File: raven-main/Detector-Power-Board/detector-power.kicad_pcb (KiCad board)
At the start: 2 copper layers, 37 x 52.5 mm, 36 parts, among them J1 DeployLipo, J2 Conn_01x06, J9 UCLipo, U1 STPS20M100SG-TR, U6 LM5185QPWPRQ1, U7 TPS7A4701xRGW, U8 TPS7A4701xRGW

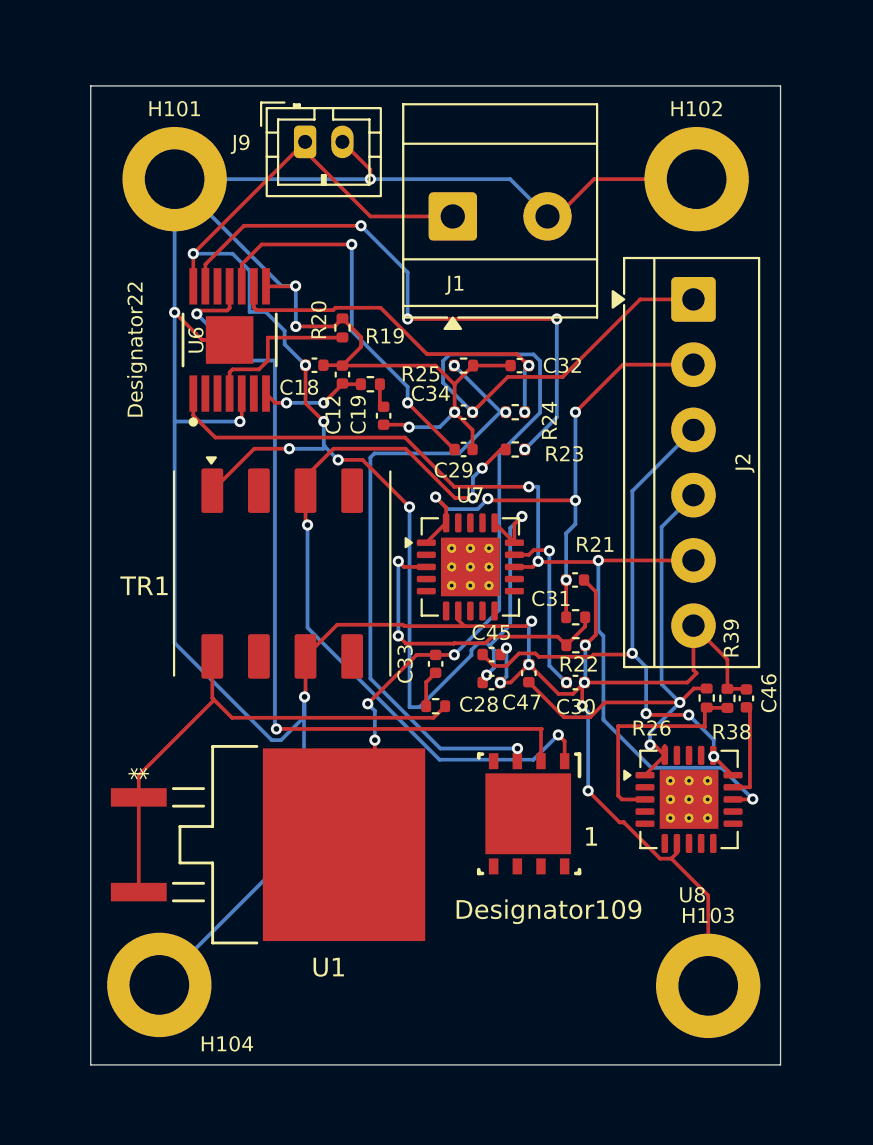
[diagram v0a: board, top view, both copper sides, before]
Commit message: Fixed Power board issues, added .step files
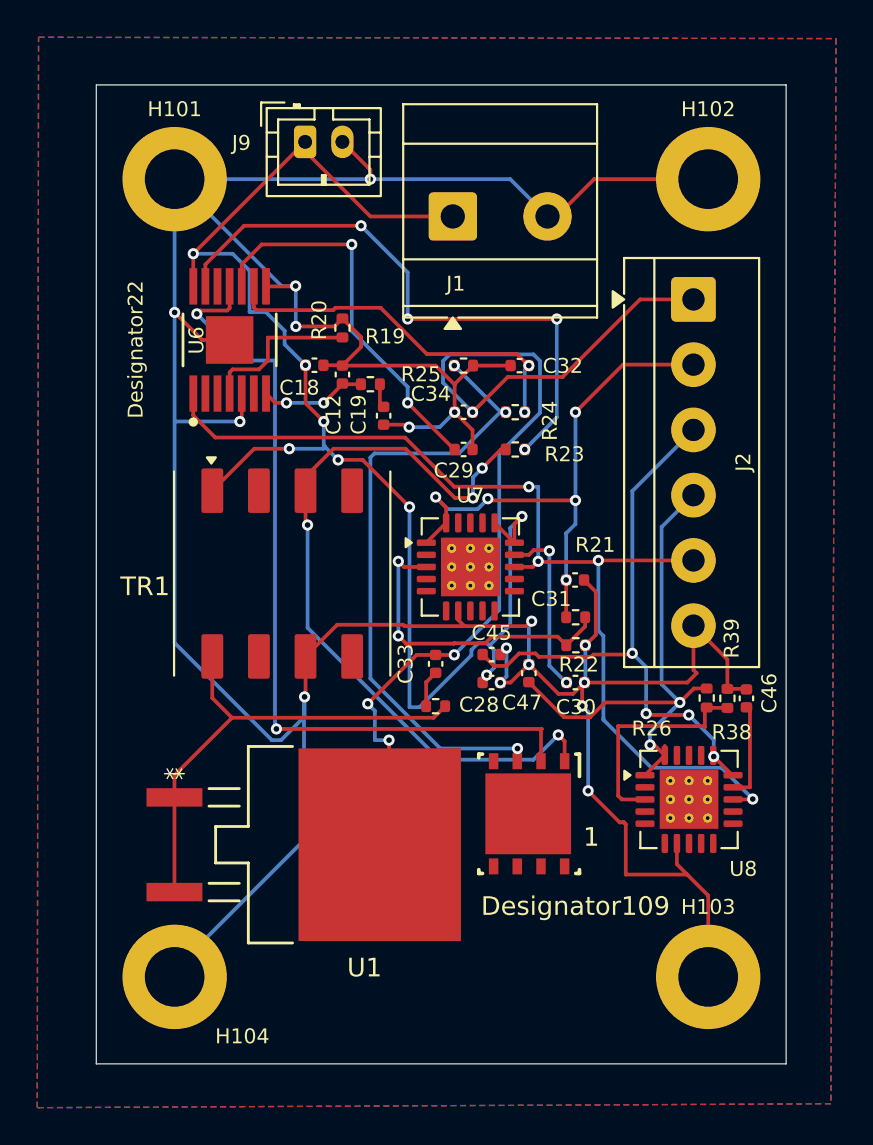
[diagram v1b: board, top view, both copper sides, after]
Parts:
- moved U1 1.91 mm to (123.8, 98.2)
- moved H104 0.93 mm to (115.0, 105.3)
- moved H102 0.62 mm to (143.6, 62.5)
- moved H103 0.48 mm to (143.6, 105.3)
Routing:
- net /Power_Out_50V: track 55.0 -> 57.7 mm
- net GND: track 201.2 -> 203.8 mm
- net Net-(R26-Pad1): track 27.4 -> 26.0 mm
- added copper zone on B.Cu, net GND
- added copper zone on F.Cu, net GND
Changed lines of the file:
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@@
 	(footprint "STPS20M100SG-TR:D2PAK_STM"
 		(layer "F.Cu")
-		(at 121.8388 98.2 -90)
+		(at 123.7521 98.2 -90)
 		(tags "STPS20M100SG-TR ")
 		(property "Reference" "U1"
@@
 		(tags "Texas VQFN NoLead")
 		(property "Reference" "U8"
-			(at 0.18 5.14 0)
+			(at 2.90875 3.72875 0)
 			(layer "F.SilkS")
 			(effects
@@
 	(footprint "MountingHole:MountingHole_3.2mm_M3_DIN965_Pad"
 		(layer "F.Cu")
-		(at 143.62 105.77)
+		(at 143.62 105.29)
 		(descr "Mounting Hole 3.2mm, M3, generated by kicad-footprint-generator mountinghole.py")
 		(tags "mountinghole M3 DIN965")
@@
 		)
 		(fp_text user "Designator109"
-			(at 5.170001 -1.045 0)
+			(at 4.960001 -2.485 0)
 			(unlocked yes)
 			(layer "F.SilkS")
@@
 	(footprint "MountingHole:MountingHole_3.2mm_M3_DIN965_Pad"
 		(layer "F.Cu")
-		(at 114.18 105.72)
+		(at 115 105.29)
 		(descr "Mounting Hole 3.2mm, M3, generated by kicad-footprint-generator mountinghole.py")
 		(tags "mountinghole M3 DIN965")
@@
 	(footprint "MountingHole:MountingHole_3.2mm_M3_DIN965_Pad"
 		(layer "F.Cu")
-		(at 143 62.5)
+		(at 143.62 62.5)
 		(descr "Mounting Hole 3.2mm, M3, generated by kicad-footprint-generator mountinghole.py")
 		(tags "mountinghole M3 DIN965")
@@
 	)
 	(gr_rect
-		(start 110.5 57.5)
-		(end 147.5 110.01)
+		(start 110.8 57.445)
+		(end 147.8 109.955)
+		(radius 5)
 		(stroke
 			(width 0.05)
-			(type default)
+			(type solid)
 		)
 		(fill no)
@@
 	)
 	(segment
+		(start 139.2 97.105432)
+		(end 139.2 99.8)
+		(width 0.2)
+		(layer "F.Cu")
+		(net "GND")
+	)
+	(segment
 		(start 144.65 89.84)
 		(end 144.65 88.27)
@@
 	)
 	(segment
+		(start 139.2 99.8)
+		(end 142.494998 99.8)
+		(width 0.2)
+		(layer "F.Cu")
+		(net "GND")
+	)
+	(segment
 		(start 130.02 73.49)
 		(end 131.01 72.5)
@@
 	)
 	(segment
-		(start 141.94125 98.646249)
-		(end 141.94125 98.13375)
-		(width 0.2)
-		(layer "F.Cu")
-		(net "GND")
-	)
-	(segment
 		(start 130.02 73.52)
 		(end 130.02 73.49)
@@
 	)
 	(segment
-		(start 141.641249 98.94625)
-		(end 143.62 100.925001)
+		(start 118.600002 75.399998)
+		(end 118.5 75.5)
 		(width 0.2)
 		(layer "F.Cu")
@@
 	)
 	(segment
-		(start 118.600002 75.399998)
-		(end 118.5 75.5)
+		(start 121.97 90.27)
+		(end 122.02 90.22)
 		(width 0.2)
 		(layer "F.Cu")
@@
 	)
 	(segment
-		(start 121.97 90.27)
-		(end 122.02 90.22)
+		(start 142.494998 99.8)
+		(end 142.497499 99.802501)
 		(width 0.2)
 		(layer "F.Cu")
@@
 	)
 	(segment
+		(start 142.497499 99.802501)
+		(end 141.94125 99.246251)
+		(width 0.2)
+		(layer "F.Cu")
+		(net "GND")
+	)
+	(segment
 		(start 130.1675 85.6625)
 		(end 130.16 85.67)
@@
 	)
 	(segment
+		(start 139.097284 97.002716)
+		(end 139.2 97.105432)
+		(width 0.2)
+		(layer "F.Cu")
+		(net "GND")
+	)
+	(segment
 		(start 137.59 84.63)
 		(end 137.59 86.94)
@@
 	)
 	(segment
-		(start 141.641249 98.94625)
-		(end 141.94125 98.646249)
-		(width 0.2)
-		(layer "F.Cu")
-		(net "GND")
-	)
-	(segment
 		(start 126.21 75.67)
 		(end 127.446671 75.67)
@@
 	)
 	(segment
-		(start 139.097284 97.002716)
-		(end 141.040818 98.94625)
-		(width 0.2)
-		(layer "F.Cu")
-		(net "GND")
-	)
-	(segment
 		(start 130.2125 85.6625)
 		(end 130.1675 85.6625)
@@
 	)
 	(segment
-		(start 141.040818 98.94625)
-		(end 141.641249 98.94625)
+		(start 130.98 75.96)
+		(end 130.02 75)
 		(width 0.2)
 		(layer "F.Cu")
@@
 	)
 	(segment
-		(start 130.98 75.96)
-		(end 130.02 75)
+		(start 141.94125 99.246251)
+		(end 141.94125 98.13375)
 		(width 0.2)
 		(layer "F.Cu")
@@
 	)
 	(segment
+		(start 143.62 100.925001)
+		(end 142.497499 99.802501)
+		(width 0.2)
+		(layer "F.Cu")
+		(net "GND")
+	)
+	(segment
 		(start 135 64.5)
 		(end 135.5 64.5)
@@
 	)
 	(segment
-		(start 117.08375 90.39625)
-		(end 117.08375 90.46625)
-		(width 0.2)
-		(layer "F.Cu")
-		(net "Net-(R26-Pad1)")
-	)
-	(segment
-		(start 128.89 91.39)
-		(end 129.51 90.77)
+		(start 117.02 90.3325)
+		(end 118.0775 91.39)
 		(width 0.2)
 		(layer "F.Cu")
@@
 	)
 	(segment
-		(start 113.0758 94.4742)
-		(end 113.0758 95.66)
+		(start 114.9891 100.74)
+		(end 114.9891 95.66)
 		(width 0.2)
 		(layer "F.Cu")
@@
 	)
 	(segment
-		(start 117.08375 90.39625)
-		(end 117.02 90.3325)
+		(start 128.89 91.39)
+		(end 129.51 90.77)
 		(width 0.2)
 		(layer "F.Cu")
@@
 	)
 	(segment
-		(start 117.08375 90.46625)
-		(end 113.0758 94.4742)
+		(start 114.9891 94.4784)
+		(end 118.0775 91.39)
 		(width 0.2)
 		(layer "F.Cu")
@@
 	)
 	(segment
-		(start 113.0758 100.74)
-		(end 113.0758 95.66)
-		(width 0.2)
-		(layer "F.Cu")
-		(net "Net-(R26-Pad1)")
-	)
-	(segment
 		(start 117.02 90.3325)
 		(end 117.02 88.1)
@@
 	)
 	(segment
-		(start 118.0775 91.39)
-		(end 117.08375 90.39625)
+		(start 114.9891 95.66)
+		(end 114.9891 94.4784)
 		(width 0.2)
 		(layer "F.Cu")
@@
 	)
 	(segment
-		(start 125.74 92.59)
-		(end 125.74 96.5467)
+		(start 126.5 97.7)
+		(end 126 98.2)
+		(width 0.2)
+		(layer "F.Cu")
+		(net "/Power_Out_50V")
+	)
+	(segment
+		(start 126.5 92.59)
+		(end 126.5 97.7)
 		(width 0.2)
 		(layer "F.Cu")
@@
 	)
 	(via
-		(at 125.74 92.59)
+		(at 125.36 90.64)
 		(size 0.6)
 		(drill 0.3)
@@
 	)
 	(via
-		(at 125.36 90.64)
+		(at 126.5 92.59)
 		(size 0.6)
 		(drill 0.3)
@@
 	)
 	(segment
+		(start 125.74 92.59)
+		(end 126.5 92.59)
+		(width 0.2)
+		(layer "B.Cu")
+		(net "/Power_Out_50V")
+	)
+	(segment
 		(start 129.4 73.42)
 		(end 129.4 72.251471)
@@
 		(net "Net-(C33-Pad1)")
 	)
+	(zone
+		(net "GND")
+		(layers "F.Cu" "B.Cu")
+		(name "Net-GND")
+		(hatch edge 0.5)
+		(connect_pads
+			(clearance 0.5)
+		)
+		(min_thickness 0.25)
+		(fill yes
+			(thermal_gap 0.5)
+			(thermal_bridge_width 0.5)
+			(island_removal_mode 0)
+		)
+		(polygon
+			(pts
+				(xy 107.7 54.89) (xy 150.48 54.96) (xy 150.201058 112.094995) (xy 107.632656 112.305037) (xy 107.7 54.9)
+			)
+		)
+	)
 	(embedded_fonts no)

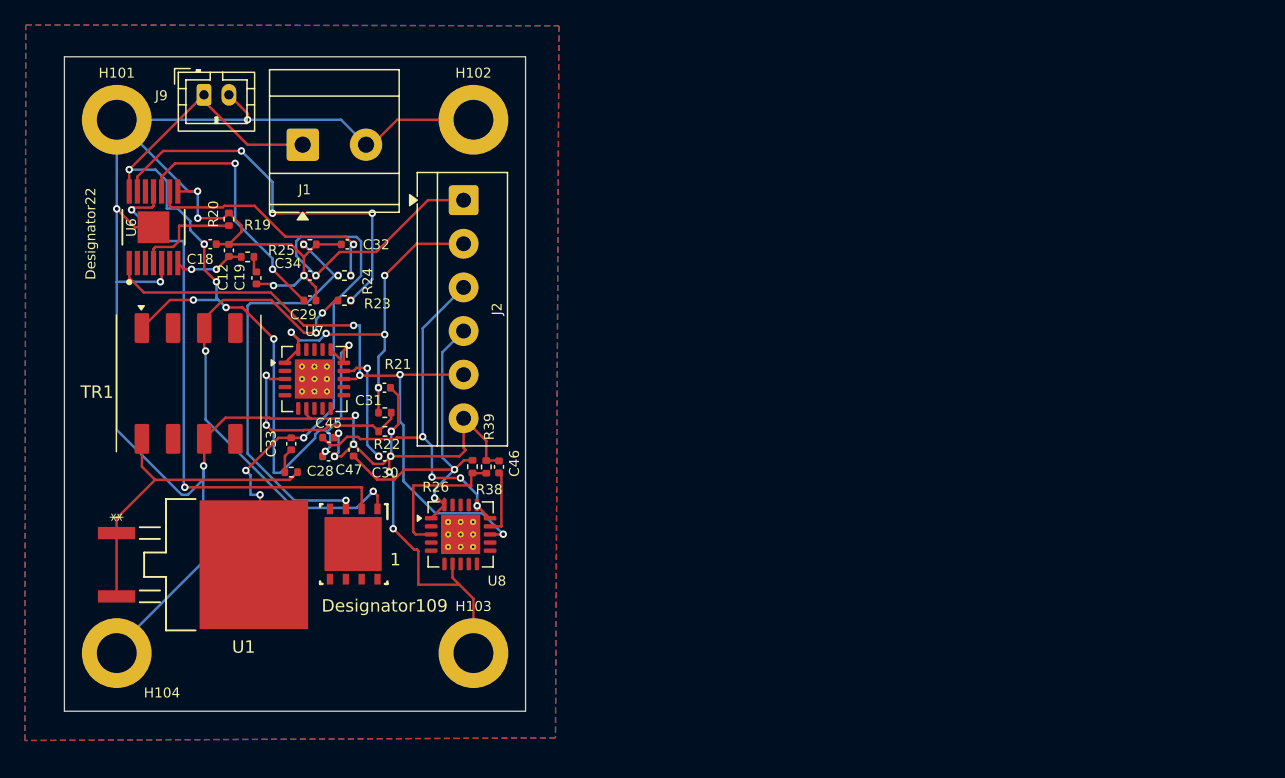
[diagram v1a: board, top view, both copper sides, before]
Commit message: Added some initial pcb changes from Revision 2
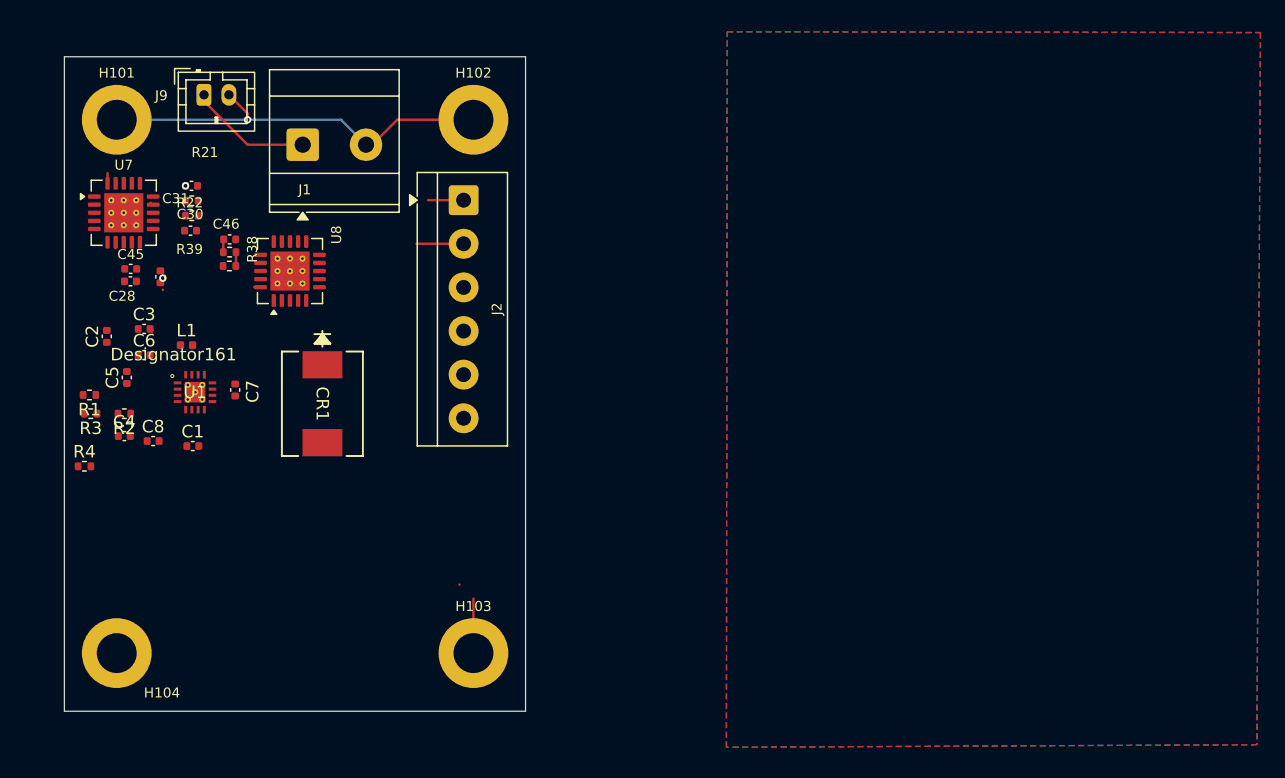
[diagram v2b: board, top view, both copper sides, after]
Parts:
- removed 1: CSD16556Q5B, ul_CSD16556Q5B:DNK0008A
- removed C12: 6.8nF, Capacitor_SMD:C_0402_1005Metric
- removed C18: 68uF, Capacitor_SMD:C_0402_1005Metric
- removed C19: 68pF, Capacitor_SMD:C_0402_1005Metric
- removed C29: 2.2uF, Capacitor_SMD:C_0402_1005Metric
- removed C32, C34: 100nF, Capacitor_SMD:C_0402_1005Metric
- removed C33: 22pF, Capacitor_SMD:C_0402_1005Metric
- removed R19: 2.05k, Resistor_SMD:R_0402_1005Metric
- removed R20: 10k, Resistor_SMD:R_0402_1005Metric
- removed R23: 10.7k, Resistor_SMD:R_0402_1005Metric
- removed R24, R26: 100, Resistor_SMD:R_0402_1005Metric
- removed R25: 20m, Resistor_SMD:R_0402_1005Metric
- removed TR1: Wurth_750319177, Transformer_SMD:Transformer_Wurth_WE-AGDT-EP7
- removed U6: LM5185QPWPRQ1, footprints:PWP0014G-IPC_A
- added C1: 1u, Capacitor_SMD:C_0402_1005Metric, F.Cu at (121.1, 88.7)
- added C2: 100n, Capacitor_SMD:C_0402_1005Metric, F.Cu at (114.2, 79.9)
- added C3: 10u, Capacitor_SMD:C_0402_1005Metric, F.Cu at (117.2, 79.3)
- added C4: 100n, Capacitor_SMD:C_0402_1005Metric, F.Cu at (115.6, 87.9)
- added C5: 15n, Capacitor_SMD:C_0402_1005Metric, F.Cu at (115.8, 83.2)
- added C6: 300p, Capacitor_SMD:C_0402_1005Metric, F.Cu at (117.2, 81.4)
- added C7: 10n, Capacitor_SMD:C_0402_1005Metric, F.Cu at (124.5, 84.2)
- added C8: 4.7u, Capacitor_SMD:C_0402_1005Metric, F.Cu at (117.9, 88.3)
- added CR1: SL43-E3/57T, SL43-E3-57T:DIODE_DO214AB, F.Cu at (131.5, 85.3)
- added L1: 2.2u, Inductor_SMD:L_0402_1005Metric, F.Cu at (120.6, 80.6)
- added R1: 845, Resistor_SMD:R_0402_1005Metric, F.Cu at (112.8, 84.6)
- added R2: 47.5k, Resistor_SMD:R_0402_1005Metric, F.Cu at (115.6, 86.1)
- added R3: 2.49k, Resistor_SMD:R_0402_1005Metric, F.Cu at (112.9, 86.1)
- added R4: 9.76k, Resistor_SMD:R_0402_1005Metric, F.Cu at (112.4, 90.3)
- U1: value STPS20M100SG-TR -> LM51571QRTERQ1; footprint STPS20M100SG-TR:D2PAK_STM -> LM51571QRTERQ1:RTE0016K
- moved C46 28.3 mm to (124.1, 72.1), turned to 180 degrees
- moved R39 26.8 mm to (124.1, 73.1), turned to 180 degrees
- moved R38 25.3 mm to (124.0, 74.2), turned to 0 degrees
- moved U8 25.2 mm to (128.9, 74.6), turned to 90 degrees
- moved C30 23.9 mm to (120.9, 71.4), turned to 180 degrees
- moved R22 23.2 mm to (121.0, 70.2), turned to 180 degrees
- moved R21 23.0 mm to (121.0, 69.0)
- moved C31 22.4 mm to (121.0, 67.8)
- moved C28 21.2 mm to (116.1, 75.5)
- moved C45 20.9 mm to (116.1, 74.5)
- moved C47 20.8 mm to (118.5, 75.1)
- moved U7 20.3 mm to (115.6, 70.0)
- moved U1 14.1 mm to (121.3, 84.4), turned to 0 degrees
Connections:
- J2 pad 1: /Power_Out_50V -> /Power_Out_25V
- U1 pad 1: Net-(R26-Pad1) -> GND
- U1 pad 2: Net-(R26-Pad1) -> Net-(U1-VCC)
- U1 pad 3: /Power_Out_50V -> /BBIN
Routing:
- net GND: track 203.8 -> 38.7 mm, vias 16 -> 1
- net /BBIN: track 77.8 -> 9.90 mm, vias 8 -> 0
- net /Power_Out_50V: track 57.7 -> 0.00 mm, vias 4 -> 0
- net /ON-OFF: track 54.5 -> 0.00 mm, vias 4 -> 0
- net Net-(1-Gate): track 44.1 -> 0.00 mm, vias 2 -> 0
- net Net-(1-Drain): track 40.8 -> 0.00 mm, vias 4 -> 0
- net Net-(1-Source): track 34.1 -> 0.00 mm, vias 3 -> 0
- net Net-(U6-FB): track 32.1 -> 0.00 mm, vias 4 -> 0
- net /Data_In_5V: track 32.2 -> 0.11 mm, vias 4 -> 0
- net /Data_Out_3V3: track 29.2 -> 0.53 mm, vias 2 -> 1
- net Net-(R26-Pad1): track 26.0 -> 0.00 mm
- net /Power_Out_5V: track 29.8 -> 4.60 mm, vias 5 -> 1
- net Net-(U6-VCC): track 20.8 -> 0.00 mm, vias 2 -> 0
- net Net-(U6-CS): track 19.9 -> 0.00 mm, vias 2 -> 0
- net Net-(U7-SENSE/FB): track 17.1 -> 0.00 mm, vias 2 -> 0
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
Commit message: Updated power circuit
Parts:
- removed CR1: SL43-E3/57T, SL43-E3-57T:DIODE_DO214AB
- removed L1: 2.2u, Inductor_SMD:L_0402_1005Metric
- removed U1: LM51571QRTERQ1, LM51571QRTERQ1:RTE0016K
- added C9: 4.7n, Capacitor_SMD:C_0402_1005Metric, F.Cu at (115.1, 88.7)
- added CR4: SL43-E3/57T, SL43-E3-57T:DIODE_DO214AB, F.Cu at (143.2, 95.3)
- added L2: DR127-3R3-R, DR127-3R3-R:DR127, F.Cu at (129.3, 99.5)
- added Q1: CSD18543Q3A, Package_SON:VSON-8_3.3x3.3mm_P0.65mm_NexFET, F.Cu at (133.9, 88.2)
- added Q2: CSD18543Q3A, Package_SON:VSON-8_3.3x3.3mm_P0.65mm_NexFET, F.Cu at (133.8, 83.9)
- added R10: 6.34k, Resistor_SMD:R_0402_1005Metric, F.Cu at (122.1, 89.7)
- added R5: 2, Resistor_SMD:R_0402_1005Metric, F.Cu at (128.6, 82.9)
- added R6: 100k, Resistor_SMD:R_0402_1005Metric, F.Cu at (122.5, 79.5)
- added R7: 191k, Resistor_SMD:R_0402_1005Metric, F.Cu at (117.5, 86.5)
- added R8: 11k, Resistor_SMD:R_0402_1005Metric, F.Cu at (119.4, 86.4)
- added R9: 105k, Resistor_SMD:R_0402_1005Metric, F.Cu at (117.7, 81.2)
- added U2: TPS43060RTE, Package_DFN_QFN:Texas_RTE_WQFN-16-1EP_3x3mm_P0.5mm_EP1.2x0.8mm_ThermalVias, F.Cu at (123.2, 83.6)
- C1: value 1u -> 100n
- C2: value 100n -> 100p
- C3: value 10u -> 100n
- C4: value 100n -> 10u
- C5: value 15n -> 10u
- C6: value 300p -> 22u
- C7: value 10n -> 8.2n
- C8: value 4.7u -> 470pF
- R1: value 845 -> 7m
- R2: value 47.5k -> 10
- R3: value 2.49k -> 10
- R4: value 9.76k -> 7m
- moved C5 21.1 mm to (136.9, 84.2), turned to -90 degrees
- moved J2 17.8 mm to (143.2, 86.7), turned to 90 degrees
- moved C6 14.4 mm to (129.7, 88.5)
- moved R3 13.9 mm to (126.5, 88.9), turned to -90 degrees
- moved R1 13.2 mm to (125.3, 88.9), turned to -90 degrees
- moved R4 11.8 mm to (124.1, 88.9), turned to -90 degrees
- moved C7 11.1 mm to (115.1, 90.1), turned to 180 degrees
- moved C3 10.3 mm to (126.8, 82.9), turned to -90 degrees
- moved C1 8.71 mm to (114.1, 83.5)
- moved C2 5.39 mm to (115.9, 85.0)
- moved C8 4.21 mm to (122.1, 88.5), turned to 180 degrees
- moved R2 3.72 mm to (112.2, 84.6), turned to 90 degrees
- moved C4 1.55 mm to (114.1, 87.4)
- moved U8 1.16 mm to (130.0, 74.4)
- moved C47 0.81 mm to (117.7, 75.0)
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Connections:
- C1 pad 1: GND -> /BBIN
- C1 pad 2: Net-(U1-VCC) -> GND
- C2 pad 1: GND -> Net-(U2-ISNS+)
- C2 pad 2: /BBIN -> Net-(U2-ISNS–)
- C3 pad 1: GND -> Net-(Q1-D)
- C3 pad 2: /Power_Out_25V -> Net-(U2-BOOT)
- C4 pad 1: GND -> Net-(C4-Pad1)
- C4 pad 2: /Power_Out_25V -> GND
- C5 pad 1: Net-(C5-Pad1) -> /Power_Out_25V
- C5 pad 2: Net-(U1-COMP) -> GND
- C6 pad 1: GND -> /BBIN
- C6 pad 2: Net-(U1-COMP) -> GND
- C7 pad 1: GND -> Net-(C7-Pad1)
- C7 pad 2: Net-(U1-SS) -> GND
- C8 pad 1: GND -> Net-(U2-COMP)
- C8 pad 2: /BBIN -> GND
- R1 pad 1: Net-(C5-Pad1) -> /BBIN
- R1 pad 2: GND -> Net-(L2-Pad1)
- R2 pad 1: /Power_Out_25V -> Net-(U2-ISNS+)
- R2 pad 2: Net-(U1-FB) -> /BBIN
- R3 pad 1: Net-(U1-FB) -> Net-(U2-ISNS–)
- R3 pad 2: GND -> Net-(L2-Pad1)
- R4 pad 1: Net-(U1-RT) -> /BBIN
- R4 pad 2: GND -> Net-(L2-Pad1)
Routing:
- net GND: track 38.7 -> 191.9 mm, vias 1 -> 12
- net /BBIN: track 9.90 -> 68.8 mm, vias 0 -> 6
- net /Power_Out_5V: track 4.60 -> 49.4 mm, vias 1 -> 4
- net Net-(C4-Pad1): track 0.00 -> 44.6 mm, vias 0 -> 4
- net /ON-OFF: track 0.00 -> 41.7 mm, vias 0 -> 3
- net /Data_In_5V: track 0.11 -> 37.6 mm, vias 0 -> 1
- net /Power_Out_25V: track 2.86 -> 40.0 mm
- net /Data_Out_3V3: track 0.53 -> 36.5 mm, vias 1 -> 4
- net Net-(U2-BOOT): track 0.00 -> 30.0 mm, vias 0 -> 2
- net Net-(Q1-D): track 0.00 -> 28.2 mm, vias 0 -> 4
- net Net-(U2-ISNS–): track 0.00 -> 16.8 mm, vias 0 -> 2
- net Net-(U7-SENSE/FB): track 0.00 -> 16.1 mm, vias 0 -> 2
- net Net-(U2-ISNS+): track 0.00 -> 13.6 mm, vias 0 -> 2
- net Net-(L2-Pad1): track 0.00 -> 12.6 mm, vias 0 -> 2
- net Net-(Q2-G): track 0.00 -> 11.8 mm, vias 0 -> 2
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
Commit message: Added draft logos to front and back
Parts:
- added G***: LOGO, Decor:iclr_logo_inverted, F.Cu at (117.0, 97.0)
- added G***: LOGO, Decor:harrier-draft, B.Cu at (130.0, 88.0)
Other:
- board text added: "Designed by Luke Pugsley"
- board text added: "Power Board for HARRIER v.1 2026"
- board text added: "Power board for Harrier v.1 2026"
